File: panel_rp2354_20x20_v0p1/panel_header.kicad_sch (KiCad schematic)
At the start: 4 parts, among them J2 Conn_01x05, J3 Conn_01x05, J4 Conn_01x05, J5 Conn_01x05

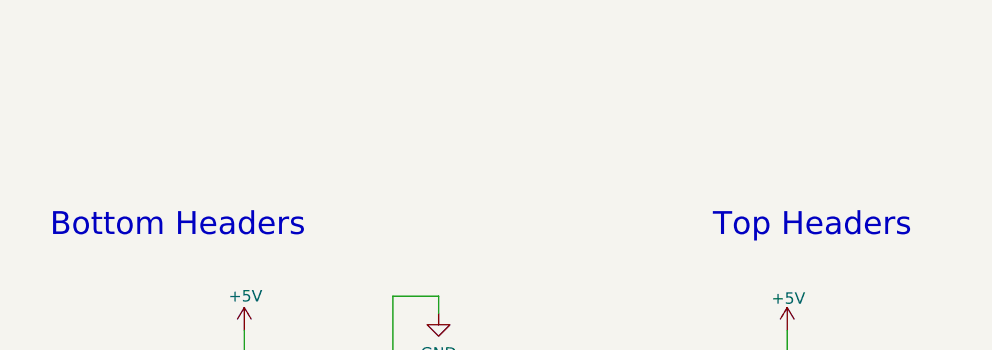
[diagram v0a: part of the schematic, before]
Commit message: Added note about EINT.
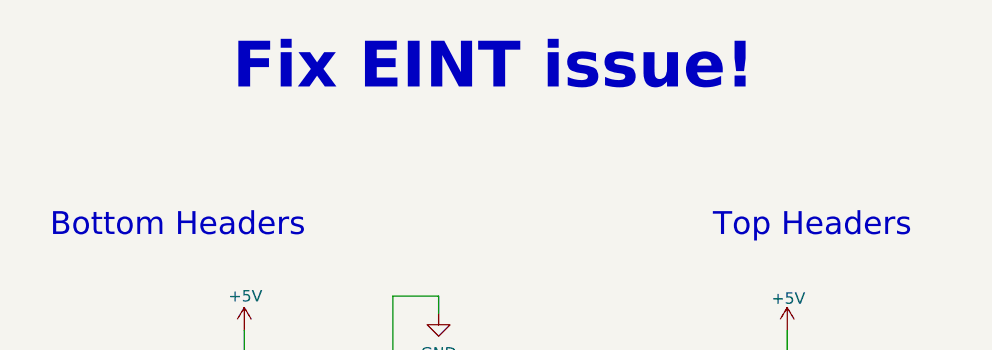
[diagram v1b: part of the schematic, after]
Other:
- note added: "Fix EINT issue!"
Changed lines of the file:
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@@
+		)
+	)
+	(text "Fix EINT issue!"
+		(exclude_from_sim no)
+		(at 136.906 52.07 0)
+		(effects
+			(font
+				(size 5.08 5.08)
+				(thickness 0.254)
+				(bold yes)
+			)
 		)
 	)

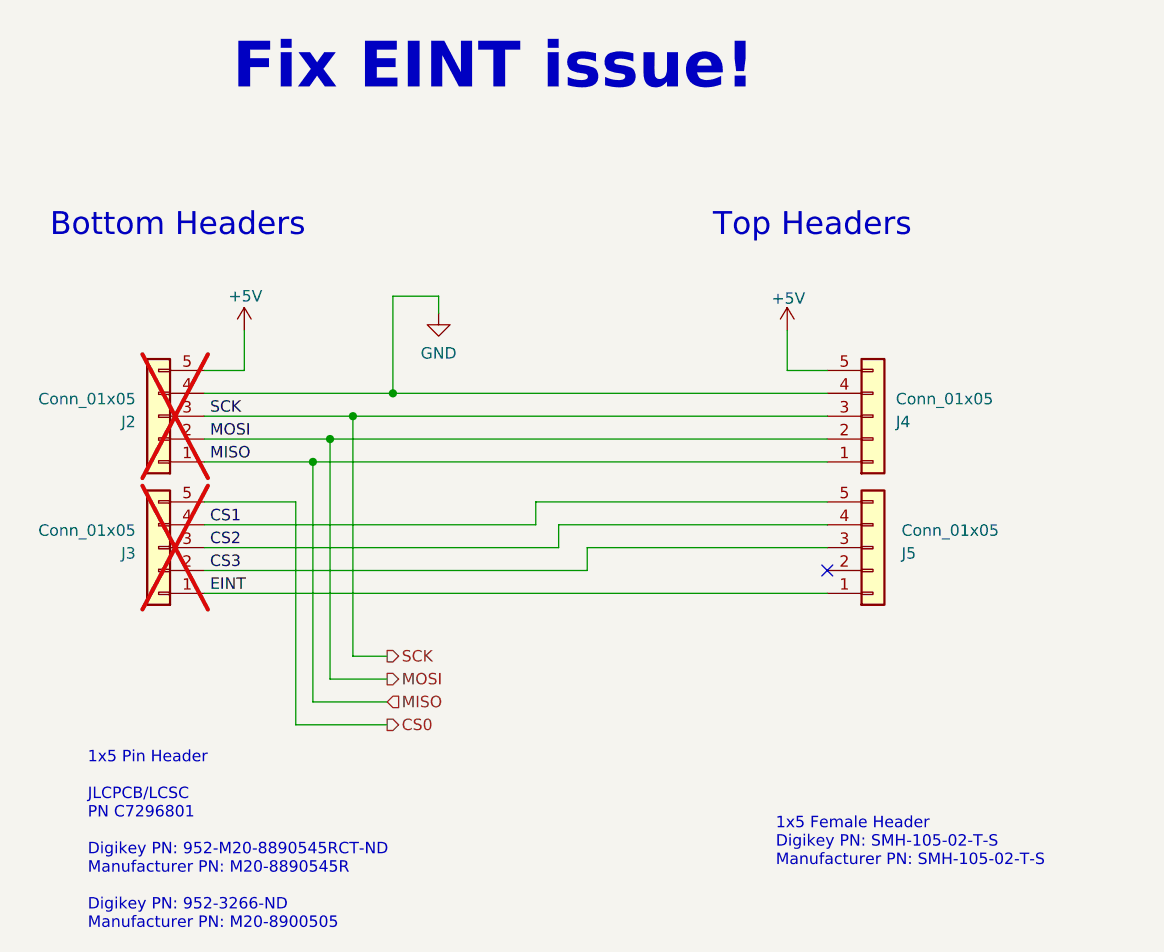
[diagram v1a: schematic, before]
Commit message: Add MISO series resistor and connect EINT to MCU
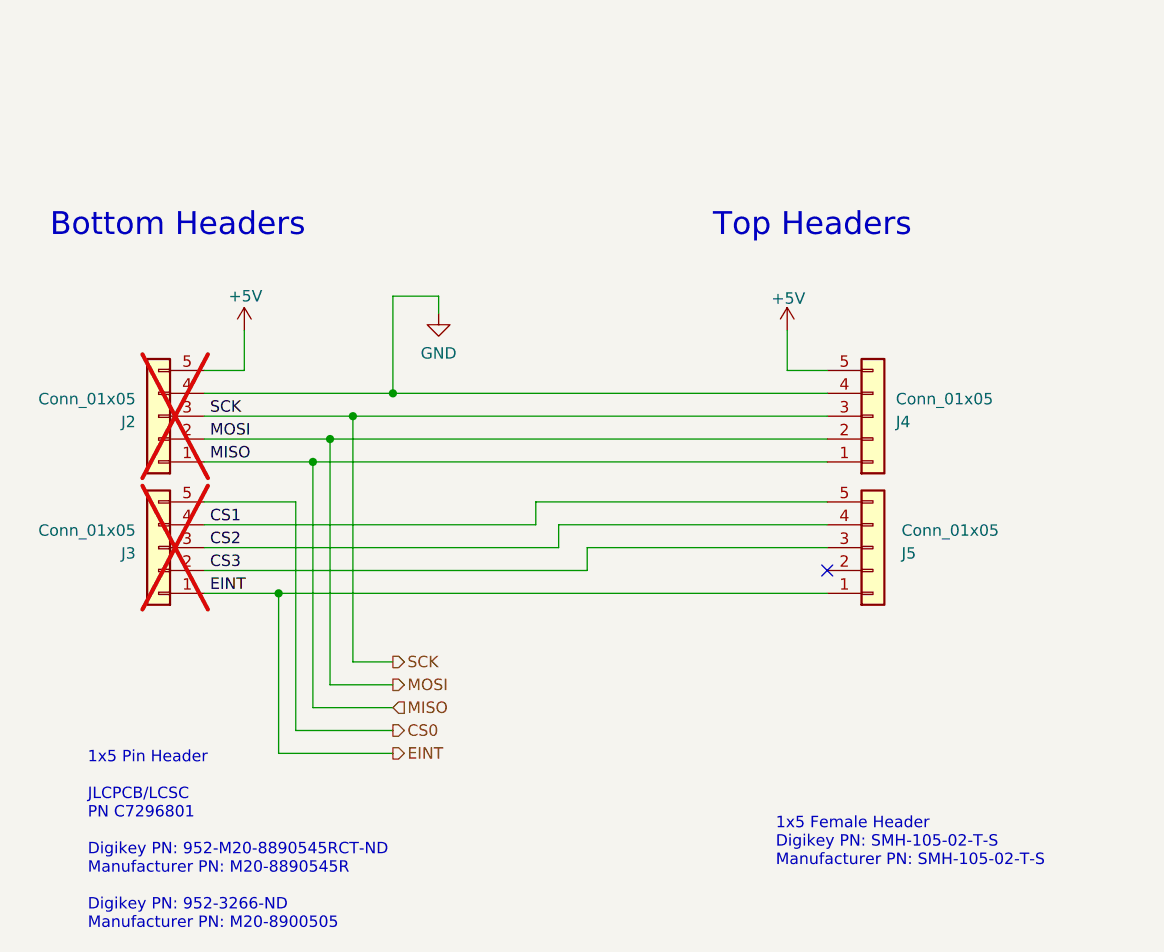
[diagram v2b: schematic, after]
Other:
- note removed: "Fix EINT issue!"
- company: (none) -> Janelia Research Campus
- title: (none) -> G6 Panel
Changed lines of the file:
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@@
 	(generator_version "9.0")
 	(paper "A4")
+	(title_block
+		(title "G6 Panel")
+		(date "2026-04-02")
+		(rev "0.2.0")
+		(company "Janelia Research Campus")
+	)
 	(text "1x5 Pin Header\n\nJLCPCB/LCSC\nPN C7296801\n\nDigikey PN: 952-M20-8890545RCT-ND\nManufacturer PN: M20-8890545R\n\nDigikey PN: 952-3266-ND\nManufacturer PN: M20-8900505"
 		(exclude_from_sim no)
@@
 			)
 			(justify left bottom)
-		)
-	)
-	(text "Fix EINT issue!"
-		(exclude_from_sim no)
-		(at 136.906 52.07 0)
-		(effects
-			(font
-				(size 5.08 5.08)
-				(thickness 0.254)
-				(bold yes)
-			)
 		)
 	)
@@
 	)
 	(junction
+		(at 113.03 110.49)
+		(diameter 0)
+		(color 0 0 0 0)
+	)
+	(junction
 		(at 121.285 90.805)
 		(diameter 0)
@@
 	(wire
 		(pts
-			(xy 125.095 125.095) (xy 114.935 125.095)
-		)
-		(stroke
-			(width 0)
-			(type default)
-		)
-	)
-	(wire
-		(pts
-			(xy 104.775 110.49) (xy 173.99 110.49)
-		)
-		(stroke
-			(width 0)
-			(type default)
-		)
-	)
-	(wire
-		(pts
-			(xy 121.285 90.805) (xy 121.285 117.475)
+			(xy 125.73 125.73) (xy 114.935 125.73)
+		)
+		(stroke
+			(width 0)
+			(type default)
+		)
+	)
+	(wire
+		(pts
+			(xy 104.775 110.49) (xy 113.03 110.49)
+		)
+		(stroke
+			(width 0)
+			(type default)
+		)
+	)
+	(wire
+		(pts
+			(xy 121.285 90.805) (xy 121.285 118.11)
 		)
 		(stroke
@@
 	(wire
 		(pts
+			(xy 113.03 128.27) (xy 125.73 128.27)
+		)
+		(stroke
+			(width 0)
+			(type default)
+		)
+	)
+	(wire
+		(pts
 			(xy 141.605 102.87) (xy 141.605 100.33)
 		)
@@
 	(wire
 		(pts
-			(xy 116.84 95.885) (xy 116.84 122.555)
+			(xy 116.84 95.885) (xy 116.84 123.19)
 		)
 		(stroke
@@
 	(wire
 		(pts
-			(xy 118.745 120.015) (xy 125.095 120.015)
+			(xy 118.745 120.65) (xy 125.73 120.65)
 		)
 		(stroke
@@
 	(wire
 		(pts
-			(xy 116.84 122.555) (xy 125.095 122.555)
+			(xy 116.84 123.19) (xy 125.73 123.19)
 		)
 		(stroke
@@
 	(wire
 		(pts
+			(xy 113.03 128.27) (xy 113.03 110.49)
+		)
+		(stroke
+			(width 0)
+			(type default)
+		)
+	)
+	(wire
+		(pts
 			(xy 104.775 105.41) (xy 144.145 105.41)
 		)
@@
 	(wire
 		(pts
-			(xy 114.935 125.095) (xy 114.935 100.33)
+			(xy 114.935 125.73) (xy 114.935 100.33)
 		)
 		(stroke
@@
 	(wire
 		(pts
-			(xy 121.285 117.475) (xy 125.095 117.475)
+			(xy 113.03 110.49) (xy 173.99 110.49)
+		)
+		(stroke
+			(width 0)
+			(type default)
+		)
+	)
+	(wire
+		(pts
+			(xy 121.285 118.11) (xy 125.73 118.11)
 		)
 		(stroke
@@
 	(wire
 		(pts
-			(xy 118.745 93.345) (xy 118.745 120.015)
+			(xy 118.745 93.345) (xy 118.745 120.65)
 		)
 		(stroke
@@
 	(hierarchical_label "CS0"
 		(shape output)
-		(at 125.095 125.095 0)
+		(at 125.73 125.73 0)
 		(effects
 			(font
@@
 	(hierarchical_label "MOSI"
 		(shape output)
-		(at 125.095 120.015 0)
+		(at 125.73 120.65 0)
+		(effects
+			(font
+				(size 1.27 1.27)
+			)
+			(justify left)
+		)
+	)
+	(hierarchical_label "EINT"
+		(shape output)
+		(at 125.73 128.27 0)
 		(effects
 			(font
@@
 	(hierarchical_label "SCK"
 		(shape output)
-		(at 125.095 117.475 0)
+		(at 125.73 118.11 0)
 		(effects
 			(font
@@
 	(hierarchical_label "MISO"
 		(shape input)
-		(at 125.095 122.555 0)
+		(at 125.73 123.19 0)
 		(effects
 			(font
@@
 		)
 		(instances
-			(project "driver_rp2350"
+			(project "panel_rp2354_20x20"
 				(path "/1e634561-32a0-4ffa-9d4f-e93f355464d5/35cc1d84-fe4a-4d4c-89d0-5c31c9afaae5"
 					(reference "#PWR0124")
@@
 		)
 		(instances
-			(project "driver_rp2350"
+			(project "panel_rp2354_20x20"
 				(path "/1e634561-32a0-4ffa-9d4f-e93f355464d5/35cc1d84-fe4a-4d4c-89d0-5c31c9afaae5"
 					(reference "#PWR0122")
@@
 		)
 		(instances
-			(project "driver_rp2350"
+			(project "panel_rp2354_20x20"
 				(path "/1e634561-32a0-4ffa-9d4f-e93f355464d5/35cc1d84-fe4a-4d4c-89d0-5c31c9afaae5"
 					(reference "#PWR0123")
@@
 		)
 		(instances
-			(project "driver_rp2350"
+			(project "panel_rp2354_20x20"
 				(path "/1e634561-32a0-4ffa-9d4f-e93f355464d5/35cc1d84-fe4a-4d4c-89d0-5c31c9afaae5"
 					(reference "J5")
@@
 		)
 		(instances
-			(project "driver_rp2350"
+			(project "panel_rp2354_20x20"
 				(path "/1e634561-32a0-4ffa-9d4f-e93f355464d5/35cc1d84-fe4a-4d4c-89d0-5c31c9afaae5"
 					(reference "J2")
@@
 		)
 		(instances
-			(project "driver_rp2350"
+			(project "panel_rp2354_20x20"
 				(path "/1e634561-32a0-4ffa-9d4f-e93f355464d5/35cc1d84-fe4a-4d4c-89d0-5c31c9afaae5"
 					(reference "J4")
@@
 		)
 		(instances
-			(project "driver_rp2350"
+			(project "panel_rp2354_20x20"
 				(path "/1e634561-32a0-4ffa-9d4f-e93f355464d5/35cc1d84-fe4a-4d4c-89d0-5c31c9afaae5"
 					(reference "J3")
